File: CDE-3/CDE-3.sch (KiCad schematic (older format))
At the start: 22 parts

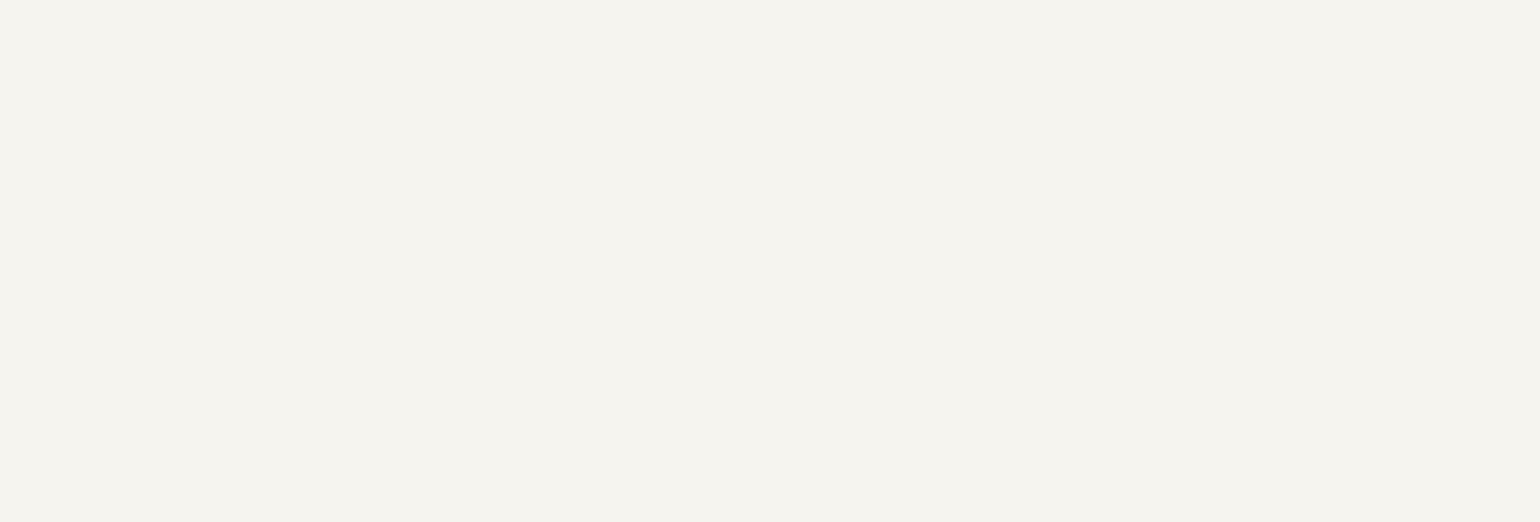
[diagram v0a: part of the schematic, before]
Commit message: iniciando o layout da PCB CDE-3
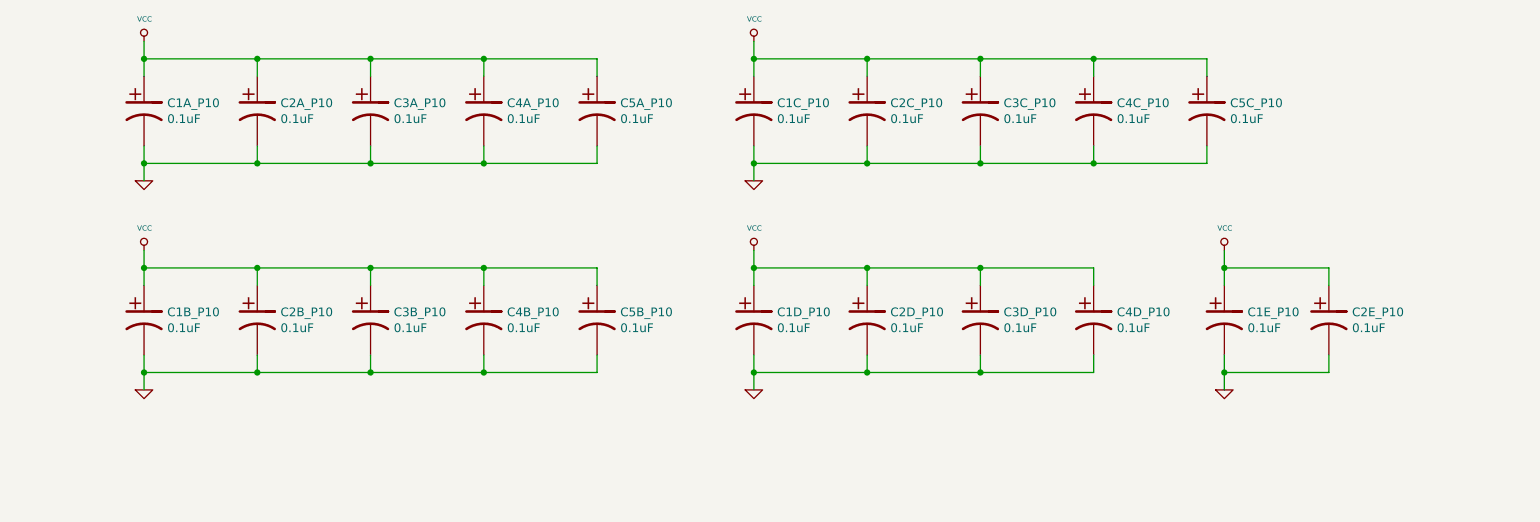
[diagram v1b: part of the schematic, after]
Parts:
- added C1A_P10, C1B_P10, C1C_P10, C1D_P10, C1E_P10, C2A_P10, C2B_P10, C2C_P10, C2D_P10, C2E_P10, C3A_P10, C3B_P10, C3C_P10, C3D_P10, C4A_P10, C4B_P10, C4C_P10, C4D_P10, C5A_P10, C5B_P10, C5C_P10: 0.1uF, Capacitors_ThroughHole:CP_Axial_L10.0mm_D4.5mm_P15.00mm_Horizontal, symbol CP1
- 1A_P10, 1B_P10, 1C_P10, 1D_P10, 1E_P10, 2A_P10, 2B_P10, 2C_P10, 2D_P10, 2E_P10, 3A_P10, 3B_P10, 3C_P10, 3D_P10, 4A_P10, 4B_P10, 4C_P10, 4D_P10, 5A_P10, 5B_P10, 5C_P10: footprint ~ -> Housings_DIP:DIP-14_W7.62mm_Socket_LongPads
- CONECTOR_P10: footprint (none) -> Pin_Headers:Pin_Header_Angled_2x35_Pitch2.54mm
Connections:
- net GND: now also C1A_P10.2, C1B_P10.2, C1C_P10.2, C1D_P10.2, C1E_P10.2, C2A_P10.2, C2B_P10.2, C2C_P10.2, C2D_P10.2, C2E_P10.2, C3A_P10.2, C3B_P10.2, C3C_P10.2, C3D_P10.2, C4A_P10.2, C4B_P10.2, C4C_P10.2, C4D_P10.2, C5A_P10.2, C5B_P10.2, C5C_P10.2
- net VCC: now also C1A_P10.1, C1B_P10.1, C1C_P10.1, C1D_P10.1, C1E_P10.1, C2A_P10.1, C2B_P10.1, C2C_P10.1, C2D_P10.1, C2E_P10.1, C3A_P10.1, C3B_P10.1, C3C_P10.1, C3D_P10.1, C4A_P10.1, C4B_P10.1, C4C_P10.1, C4D_P10.1, C5A_P10.1, C5B_P10.1, C5C_P10.1

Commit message: update schematics symbols on CDE-3 after installing kicad compiled from today's git master source code.
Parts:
- 1A_P10, 1B_P10, 2A_P10, 2B_P10, 3A_P10, 3B_P10: symbol 74HC04 -> CDE-3-rescue:74HC04-RESCUE-CDE-3
- 1C_P10, 1D_P10, 1E_P10, 2D_P10, 3D_P10: symbol 74LS10 -> CDE-3-rescue:74LS10-RESCUE-CDE-3
- 2C_P10: symbol 74LS30 -> CDE-3-rescue:74LS30-RESCUE-CDE-3
- 2E_P10: symbol 74LS13 -> CDE-3-rescue:74LS13-RESCUE-CDE-3
- 3C_P10, 4A_P10, 4B_P10, 4C_P10, 5A_P10, 5B_P10, 5C_P10: symbol 7402 -> CDE-3-rescue:7402-RESCUE-CDE-3
- 4D_P10: symbol 7400 -> CDE-3-rescue:7400-RESCUE-CDE-3
- C1A_P10, C1B_P10, C1C_P10, C1D_P10, C1E_P10, C2A_P10, C2B_P10, C2C_P10, C2D_P10, C2E_P10, C3A_P10, C3B_P10, C3C_P10, C3D_P10, C4A_P10, C4B_P10, C4C_P10, C4D_P10, C5A_P10, C5B_P10, C5C_P10: symbol CP1 -> CDE-3-rescue:CP1-RESCUE-CDE-3
- CONECTOR_P10: symbol CONN_35X2 -> CDE-3-rescue:CONN_35X2-RESCUE-CDE-3
